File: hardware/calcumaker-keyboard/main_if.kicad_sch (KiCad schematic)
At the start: 1 part, among them J1 TO MCU

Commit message: hardware: MCU -> STM32U575RGT6 (LQFP-64) + 4MB QSPI flash; monospace wiring notes
MCU package + external flash
- Swap U1 STM32U575ZGT6 (LQFP-144) -> STM32U575RGT6 (LQFP-64, LCSC C5270980).
  The firmware links at ~323 KB so 1 MB flash is ample (~3x headroom), and with
  the key matrix scanned off-board the LQFP-64 has enough GPIO — smaller/cheaper.
- Correct the flash size everywhere: the STM32 `G` code = 1 MB (not 2 MB; the
  `I` parts are 2 MB). memory.x FLASH 2048K -> 1024K; .cargo runner -> RGTx.
- Add U7 W25Q32JVSSIQ, a 4 MB (32 Mbit) quad-SPI NOR (LCSC C179173, SOIC-8) on
  OCTOSPI1 as a new QSPIFlash sheet (+ R9 CS# pull-up + C26 decoupling) for
  memory-mapped (XIP) constants + state/program storage.
- mcu board 52 -> 55 components / 7 sheets. Docs (DESIGN.md, PARTS.md, READMEs,
  CLAUDE/AGENTS) updated; availability ladder now lists RGT6/VGT6/ZGT6.

Monospace, multi-line schematic wiring notes
- kschgen text_note() now renders notes in a monospace font (Courier New) so
  tables/columns line up; add note_block() + pin_table() helpers.
- Reformat all 14 per-sheet notes into titled, multi-line, aligned blocks —
  connector pinouts as PIN/SIGNAL tables, power/MCU sheets as wiring blocks.

The regenerated schematics carry both changes, so this is one commit. All three
boards regenerate + pass the structure check (mcu 55 / keyboard 119 / display
60, no duplicate refs).

Co-Authored-By: Claude Opus 4.8 (1M context) <noreply@anthropic.com>
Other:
- note added: "MCU MEZZANINE - J1 DF40C-10DP-0.4V (LCSC C424635) Hirose DF40 2x5 0.4mm HEADER; mates DOWN to the MCU-board receptacle (mcu J5 DF40C-10DS, C424636). Low-profile 1.5mm stack. PLACED, not wired. PINOUT MUST match mcu J5 exactly (mated pin N <-> N): PIN SIGNAL PIN SIGNAL 1 +3V3 6 KB_UART_RX 2 GND 7 KB_IRQ 3 I2C_SDA 8 KB_NRST 4 I2C_SCL 9 KB_BOOT0 5 KB_UART_TX 10 GND SDA/SCL <-> the G0 I2C1; UART_TX/R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"
- note removed: "Calcumaker 16 keyboard — MCU mezzanine (J1 = Hirose DF40 2x5 0.4mm HEADER DF40C-10DP-0.4V, LCSC C424635). Mates DOWN to the MCU board's receptacle (calcumaker-mcu J5 DF40C-10DS-0.4V C424636); LOW-PROFILE 1.5mm stack. PLACED, not wired. PINOUT (MUST match calcumaker-mcu J5 exactly): 1=+3V3, 2=GND, 3=I2C_SDA, 4=I2C_SCL, 5=KB_UART_TX, 6=KB_UART_RX, 7=KB_IRQ, 8=KB_NRST, 9=KB_BOOT0, 10=GND. SDA/SCL <-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"
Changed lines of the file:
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@@
 		(instances
 			(project "calcumaker-keyboard"
-				(path "/ca1c0000-0000-4000-8000-00000000eb01/35d144ad-c1bb-47ad-89df-34abbc593a21"
+				(path "/ca1c0000-0000-4000-8000-00000000eb01/b7ee0e1e-9650-4819-94f9-be2379d6e47b"
 					(reference "J1")
 					(unit 1)
@@
 		)
 	)
-	(text "Calcumaker 16 keyboard — MCU mezzanine (J1 = Hirose DF40 2x5 0.4mm HEADER DF40C-10DP-0.4V, LCSC C424635). Mates DOWN to the MCU board's receptacle (calcumaker-mcu J5 DF40C-10DS-0.4V C424636); LOW-PROFILE 1.5mm stack. PLACED, not wired. PINOUT (MUST match calcumaker-mcu J5 exactly): 1=+3V3, 2=GND, 3=I2C_SDA, 4=I2C_SCL, 5=KB_UART_TX, 6=KB_UART_RX, 7=KB_IRQ, 8=KB_NRST, 9=KB_BOOT0, 10=GND. SDA/SCL <-> the G0's I2C1; UART_TX/RX <-> the G0's USART; KB_IRQ = G0 -> U575 wake (keypress); KB_NRST/KB_BOOT0 = U575 -> G0 (reset + bootloader reflash). MECH: at 1.5mm stack keep the MX pins off the MCU-board area (trim, or MCU board under a keyless region). Verify DF40C-10DP land vs the KiCad DF40 2x5 footprint + the 3D stack at layout. See DESIGN.md Board Partition + Low-power & wake."
+	(text "MCU MEZZANINE  -  J1  DF40C-10DP-0.4V  (LCSC C424635)\nHirose DF40 2x5 0.4mm HEADER; mates DOWN to the MCU-board receptacle\n(mcu J5 DF40C-10DS, C424636).  Low-profile 1.5mm stack.  PLACED, not wired.\nPINOUT MUST match mcu J5 exactly (mated pin N <-> N):\n\n  PIN  SIGNAL        PIN  SIGNAL    \n    1  +3V3            6  KB_UART_RX\n    2  GND             7  KB_IRQ    \n    3  I2C_SDA         8  KB_NRST   \n    4  I2C_SCL         9  KB_BOOT0  \n    5  KB_UART_TX     10  GND\n\nSDA/SCL <-> the G0 I2C1;  UART_TX/RX <-> the G0 USART.\nKB_IRQ  = G0 -> U575 wake (keypress).\nKB_NRST / KB_BOOT0 = U575 -> G0 (reset + bootloader reflash).\nMECH: at 1.5mm stack keep MX pins off the MCU-board area (trim, or MCU\nboard under a keyless region).\nVerify DF40C-10DP land vs the KiCad DF40 2x5 fp + 3D stack at layout."
 		(exclude_from_sim no)
 		(at 15.00 105.00 0)
-		(effects (font (size 1.5 1.5)) (justify left top))
+		(effects (font (face "Courier New") (size 1.27 1.27)) (justify left top))
 	)
 	(sheet_instances

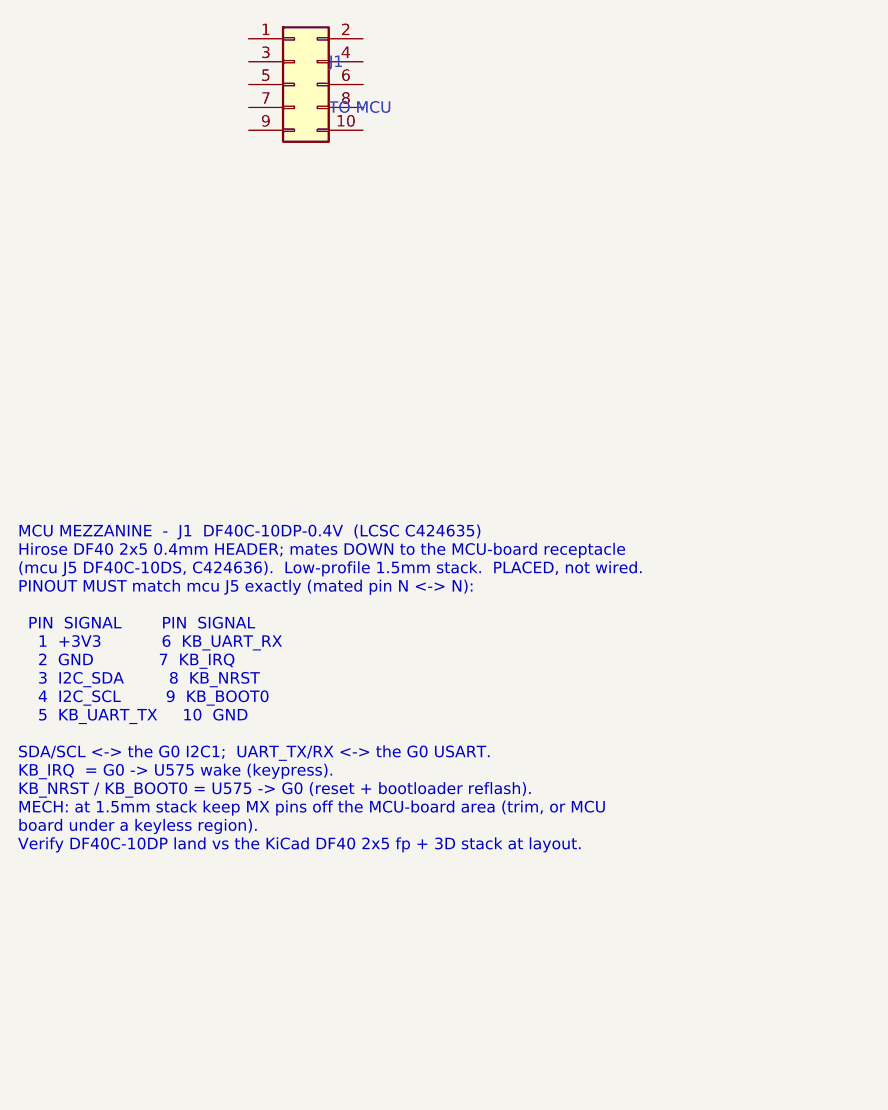
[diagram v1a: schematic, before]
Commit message: hardware: per-key RGB hint lighting on the keyboard board (50x SK6805 on gated VSYS) (#4)
Add addressable RGB accent lighting that hints key positions / presses -- one
SK6805-EC15 (1.5x1.5mm, the smallest serial RGB with a KiCad footprint + real
LCSC stock, C2890035) beside each of the 50 keys, single-wire daisy chain off
one STM32G0 pin.

Power: the LEDs are ~5V parts and the keyboard rail is only 3.3V, so they run
off VSYS (the MCU board's load-shared battery/USB rail, ~3.7-4.7V) brought up a
WIDENED 12-pin mezzanine (10 -> 12: +VSYS +GND). A high-side P-FET load switch
(Q1 AO3401A + Q2 2N7002) gates the whole LED rail off in sleep (G0 LED_EN) to
protect battery life, and a 74LVC1G125 (powered from the gated rail) level-shifts
the 3.3V data up to the LED VIH.

- calcumaker-keyboard: new KeyLighting sheet (50x SK6805 D56-D105 + U2 shifter +
  Q1/Q2 load switch + R7-R10 / C6-C7); J1 mezzanine -> 12-pin DF40C-12DP
  (C6224952). 119 -> 178 components.
- calcumaker-mcu: J5 mezzanine -> 12-pin DF40B-12DS (C3641147); route VSYS.
- DF40 stack: the receptacle SUFFIX sets the mated height (none = 1.5mm,
  (2.0) = 2.0mm, H-series = 2.5-4.0mm), NOT the B/C letter; the DF40C plug is the
  common header -- so DF40C-12DP x DF40B-12DS is a valid 1.5mm stack, same as the
  original 10-pin (DF40C-12DS just isn't LCSC-stocked).
- DESIGN.md / PARTS.md / memory: RGB subsystem, 12-pin pinout, BOM rows, the
  sleep-gate + current-cap notes (firmware must cap total brightness; 50x
  full-white ~0.75A would exceed the DF40 / VSYS budget).

All three boards regenerate + pass the structure check (mcu 55 / keyboard 178 /
display 60, no duplicate refs).

Co-authored-by: Claude Opus 4.8 (1M context) <noreply@anthropic.com>
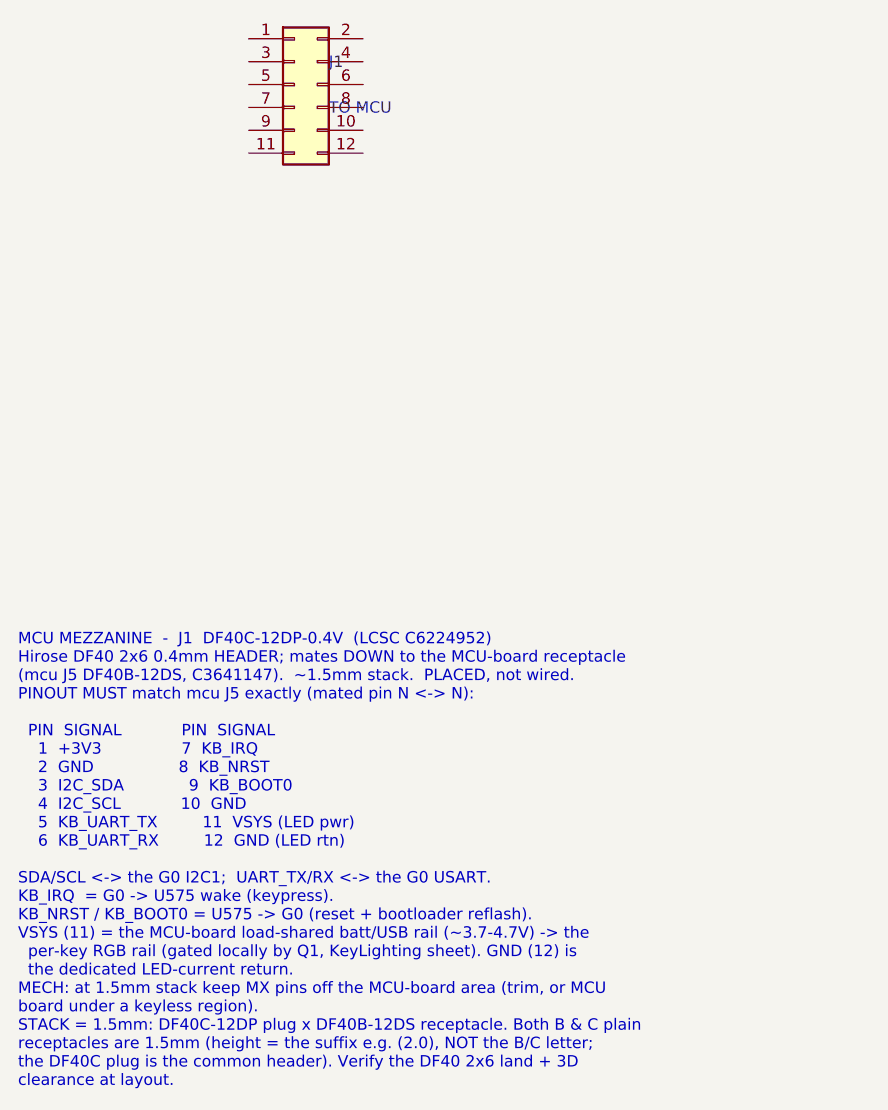
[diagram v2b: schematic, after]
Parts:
- removed J1: TO MCU, Connector_Hirose_DF40:Hirose_DF40C-10DP-0.4V_2x05-1MP_P0.4mm, symbol Connector_Generic:Conn_02x05_Odd_Even
- added J1: TO MCU, Connector_Hirose_DF40:Hirose_DF40C-12DP-0.4V_2x06-1MP_P0.4mm, symbol Connector_Generic:Conn_02x06_Odd_Even
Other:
- note added: "MCU MEZZANINE - J1 DF40C-12DP-0.4V (LCSC C6224952) Hirose DF40 2x6 0.4mm HEADER; mates DOWN to the MCU-board receptacle (mcu J5 DF40B-12DS, C3641147). ~1.5mm stack. PLACED, not wired. PINOUT MUST match mcu J5 exactly (mated pin N <-> N): PIN SIGNAL PIN SIGNAL 1 +3V3 7 KB_IRQ 2 GND 8 KB_NRST 3 I2C_SDA 9 KB_BOOT0 4 I2C_SCL 10 GND 5 KB_UART_TX 11 VSYS (LED pwr) 6 KB_UART_RX 12 GND (LED rtn) SDA/SCL 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"
- note removed: "MCU MEZZANINE - J1 DF40C-10DP-0.4V (LCSC C424635) Hirose DF40 2x5 0.4mm HEADER; mates DOWN to the MCU-board receptacle (mcu J5 DF40C-10DS, C424636). Low-profile 1.5mm stack. PLACED, not wired. PINOUT MUST match mcu J5 exactly (mated pin N <-> N): PIN SIGNAL PIN SIGNAL 1 +3V3 6 KB_UART_RX 2 GND 7 KB_IRQ 3 I2C_SDA 8 KB_NRST 4 I2C_SCL 9 KB_BOOT0 5 KB_UART_TX 10 GND SDA/SCL <-> the G0 I2C1; UART_TX/R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"
- title: Calcumaker 16 — Keyboard — MCU mezzanine (I2C + UART link down to the MCU board) -> Calcumaker 16 — Keyboard — MCU mezzanine (I2C + UART + VSYS down to the MCU board)
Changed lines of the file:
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@@
 	(paper "A3")
 	(title_block
-		(title "Calcumaker 16 — Keyboard — MCU mezzanine (I2C + UART link down to the MCU board)")
-		(date "2026-07-05")
-		(rev "0.2")
+		(title "Calcumaker 16 — Keyboard — MCU mezzanine (I2C + UART + VSYS down to the MCU board)")
+		(date "2026-07-06")
+		(rev "0.3")
 		(company "calcumaker authors")
 	)
 	(symbol
-		(lib_id "Connector_Generic:Conn_02x05_Odd_Even")
+		(lib_id "Connector_Generic:Conn_02x06_Odd_Even")
 		(at 45.7200 55.8800 0)
 		(unit 1)
@@
 			(effects (font (size 1.27 1.27)) (justify left))
 		)
-		(property "Footprint" "Connector_Hirose_DF40:Hirose_DF40C-10DP-0.4V_2x05-1MP_P0.4mm"
+		(property "Footprint" "Connector_Hirose_DF40:Hirose_DF40C-12DP-0.4V_2x06-1MP_P0.4mm"
 			(at 45.7200 55.8800 0)
 			(effects (font (size 1.27 1.27))) (hide yes)
@@
 			(effects (font (size 1.27 1.27))) (hide yes)
 		)
-		(property "LCSC" "C424635"
+		(property "LCSC" "C6224952"
 			(at 45.7200 55.8800 0)
 			(effects (font (size 1.27 1.27))) (hide yes)
 		)
-		(property "MPN" "DF40C-10DP-0.4V(51)"
+		(property "MPN" "DF40C-12DP-0.4V(51)"
 			(at 45.7200 55.8800 0)
 			(effects (font (size 1.27 1.27))) (hide yes)
@@
 		(pin "9")
 		(pin "10")
+		(pin "11")
+		(pin "12")
 		(instances
 			(project "calcumaker-keyboard"
@@
 		)
 	)
-	(text "MCU MEZZANINE  -  J1  DF40C-10DP-0.4V  (LCSC C424635)\nHirose DF40 2x5 0.4mm HEADER; mates DOWN to the MCU-board receptacle\n(mcu J5 DF40C-10DS, C424636).  Low-profile 1.5mm stack.  PLACED, not wired.\nPINOUT MUST match mcu J5 exactly (mated pin N <-> N):\n\n  PIN  SIGNAL        PIN  SIGNAL    \n    1  +3V3            6  KB_UART_RX\n    2  GND             7  KB_IRQ    \n    3  I2C_SDA         8  KB_NRST   \n    4  I2C_SCL         9  KB_BOOT0  \n    5  KB_UART_TX     10  GND\n\nSDA/SCL <-> the G0 I2C1;  UART_TX/RX <-> the G0 USART.\nKB_IRQ  = G0 -> U575 wake (keypress).\nKB_NRST / KB_BOOT0 = U575 -> G0 (reset + bootloader reflash).\nMECH: at 1.5mm stack keep MX pins off the MCU-board area (trim, or MCU\nboard under a keyless region).\nVerify DF40C-10DP land vs the KiCad DF40 2x5 fp + 3D stack at layout."
+	(text "MCU MEZZANINE  -  J1  DF40C-12DP-0.4V  (LCSC C6224952)\nHirose DF40 2x6 0.4mm HEADER; mates DOWN to the MCU-board receptacle\n(mcu J5 DF40B-12DS, C3641147).  ~1.5mm stack.  PLACED, not wired.\nPINOUT MUST match mcu J5 exactly (mated pin N <-> N):\n\n  PIN  SIGNAL            PIN  SIGNAL        \n    1  +3V3                7  KB_IRQ        \n    2  GND                 8  KB_NRST       \n    3  I2C_SDA             9  KB_BOOT0      \n    4  I2C_SCL            10  GND           \n    5  KB_UART_TX         11  VSYS (LED pwr)\n    6  KB_UART_RX         12  GND (LED rtn)\n\nSDA/SCL <-> the G0 I2C1;  UART_TX/RX <-> the G0 USART.\nKB_IRQ  = G0 -> U575 wake (keypress).\nKB_NRST / KB_BOOT0 = U575 -> G0 (reset + bootloader reflash).\nVSYS (11) = the MCU-board load-shared batt/USB rail (~3.7-4.7V) -> the\n  per-key RGB rail (gated locally by Q1, KeyLighting sheet). GND (12) is\n  the dedicated LED-current return.\nMECH: at 1.5mm stack keep MX pins off the MCU-board area (trim, or MCU\nboard under a keyless region).\nSTACK = 1.5mm: DF40C-12DP plug x DF40B-12DS receptacle. Both B & C plain\nreceptacles are 1.5mm (height = the suffix e.g. (2.0), NOT the B/C letter;\nthe DF40C plug is the common header). Verify the DF40 2x6 land + 3D\nclearance at layout."
 		(exclude_from_sim no)
-		(at 15.00 105.00 0)
+		(at 15.00 116.88 0)
 		(effects (font (face "Courier New") (size 1.27 1.27)) (justify left top))
 	)
